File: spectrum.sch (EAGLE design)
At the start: 38 parts, among them CN1 PH-1X06RG, CN2 PH-1X04SG, CN3 PH-1X04SG, CN4 FH-1X06RG, IC1 7W14FU, IC2 7W14FU, IC3 7W14FU, IC5 NJM2670E3, IC6 NJM2670E3, IC7 NJM2670E3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

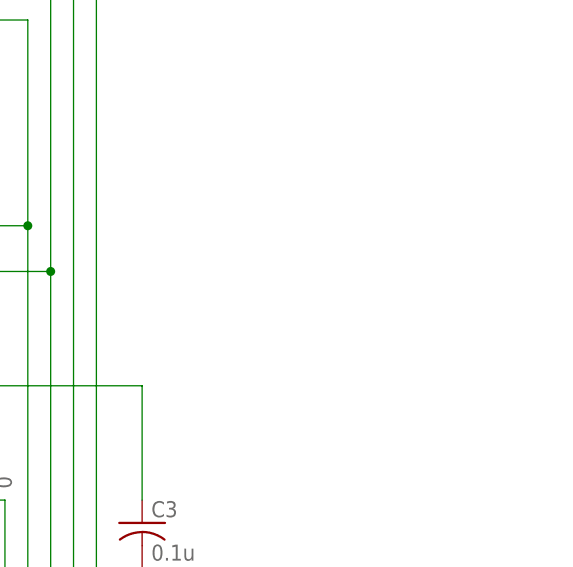
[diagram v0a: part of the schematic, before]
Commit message: Added power chains
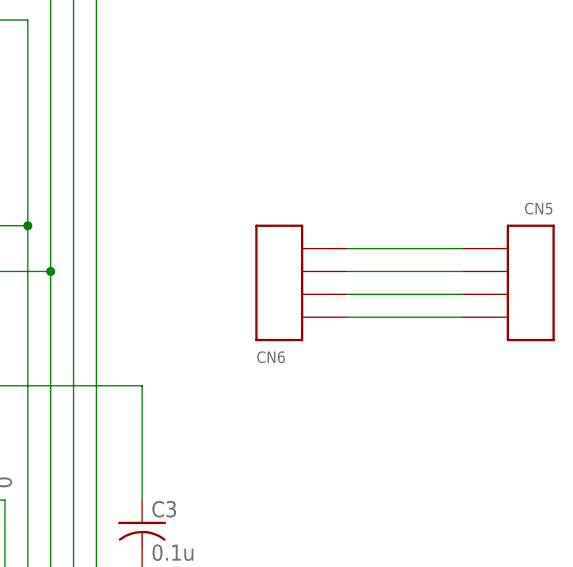
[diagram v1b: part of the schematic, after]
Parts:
- added CN5: PH-1X04SGRG, MyLib:PH-1X04SGRG
- added CN6: FH-1X04RG, MyLib:FH-1X04RG
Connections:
- new net N$42: CN5.P$3, CN6.P$2
- new net N$43: CN5.P$2, CN6.P$3
- new net N$45: CN5.P$1, CN6.P$4
- new net N$46: CN5.P$4, CN6.P$1
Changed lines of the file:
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@@
 <part name="C4" library="MyLib" deviceset="C" device="2012" value="0.1u"/>
 <part name="C5" library="MyLib" deviceset="C" device="2012" value="0.1u"/>
+<part name="CN5" library="MyLib" deviceset="PH-1X04SG" device="RG"/>
+<part name="CN6" library="MyLib" deviceset="FH-1X04" device="RG"/>
 </parts>
 <sheets>
@@
 <instance part="C4" gate="G$1" x="48.26" y="134.62"/>
 <instance part="C5" gate="G$1" x="48.26" y="180.34"/>
+<instance part="CN5" gate="G$1" x="91.44" y="93.98" rot="R180"/>
+<instance part="CN6" gate="G$1" x="63.5" y="96.52"/>
 </instances>
 <busses>
@@
 </segment>
 </net>
+<net name="N$42" class="0">
+<segment>
+<pinref part="CN6" gate="G$1" pin="P$2"/>
+<pinref part="CN5" gate="G$1" pin="P$3"/>
+<wire x1="71.12" y1="96.52" x2="83.82" y2="96.52" width="0.1524" layer="91"/>
+</segment>
+</net>
+<net name="N$43" class="0">
+<segment>
+<pinref part="CN6" gate="G$1" pin="P$3"/>
+<pinref part="CN5" gate="G$1" pin="P$2"/>
+<wire x1="71.12" y1="93.98" x2="83.82" y2="93.98" width="0.1524" layer="91"/>
+</segment>
+</net>
+<net name="N$45" class="0">
+<segment>
+<pinref part="CN6" gate="G$1" pin="P$4"/>
+<pinref part="CN5" gate="G$1" pin="P$1"/>
+<wire x1="71.12" y1="91.44" x2="83.82" y2="91.44" width="0.1524" layer="91"/>
+</segment>
+</net>
+<net name="N$46" class="0">
+<segment>
+<pinref part="CN6" gate="G$1" pin="P$1"/>
+<pinref part="CN5" gate="G$1" pin="P$4"/>
+<wire x1="71.12" y1="99.06" x2="83.82" y2="99.06" width="0.1524" layer="91"/>
+</segment>
+</net>

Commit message: Complete routing for the first time
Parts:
- added C6: 1500u, MyLib:CCE3.5-8
- added R21, R22, R23, R24, R25: 0, MyLib:R0204/7
- added R26: 0, MyLib:R0204/5
- R20: device MyLib:R2012 -> MyLib:R0204/5
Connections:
- removed net N$44: IC8.!RESET!, R20.2
- new net N$47: IC7.VS_B, R25.1
- net GND: now also C6.-, CN5.P$2, CN5.P$3, CN6.P$2, CN6.P$3, R20.1, R20.2, R26.1, R26.2
- net N$13: now also C6.+, CN5.P$1, CN5.P$4, CN6.P$1, CN6.P$4, R21.1, R22.2, R23.2, R24.2, R25.2; no longer IC5.VS_B, IC6.VS_A, IC6.VS_B, IC7.VS_A, IC7.VS_B
- net N$42: now also IC5.VS_B, R21.2; no longer CN5.P$3, CN6.P$2
- net N$43: now also IC6.VS_A, R22.1; no longer CN5.P$2, CN6.P$3
- net N$45: now also IC6.VS_B, R23.1; no longer CN5.P$1, CN6.P$4
- net N$46: now also IC7.VS_A, R24.1; no longer CN5.P$4, CN6.P$1
- net RESET: now also IC8.!RESET!; no longer R20.1
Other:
- moved on the sheet: R20
